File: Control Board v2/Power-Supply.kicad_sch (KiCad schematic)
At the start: 0 parts

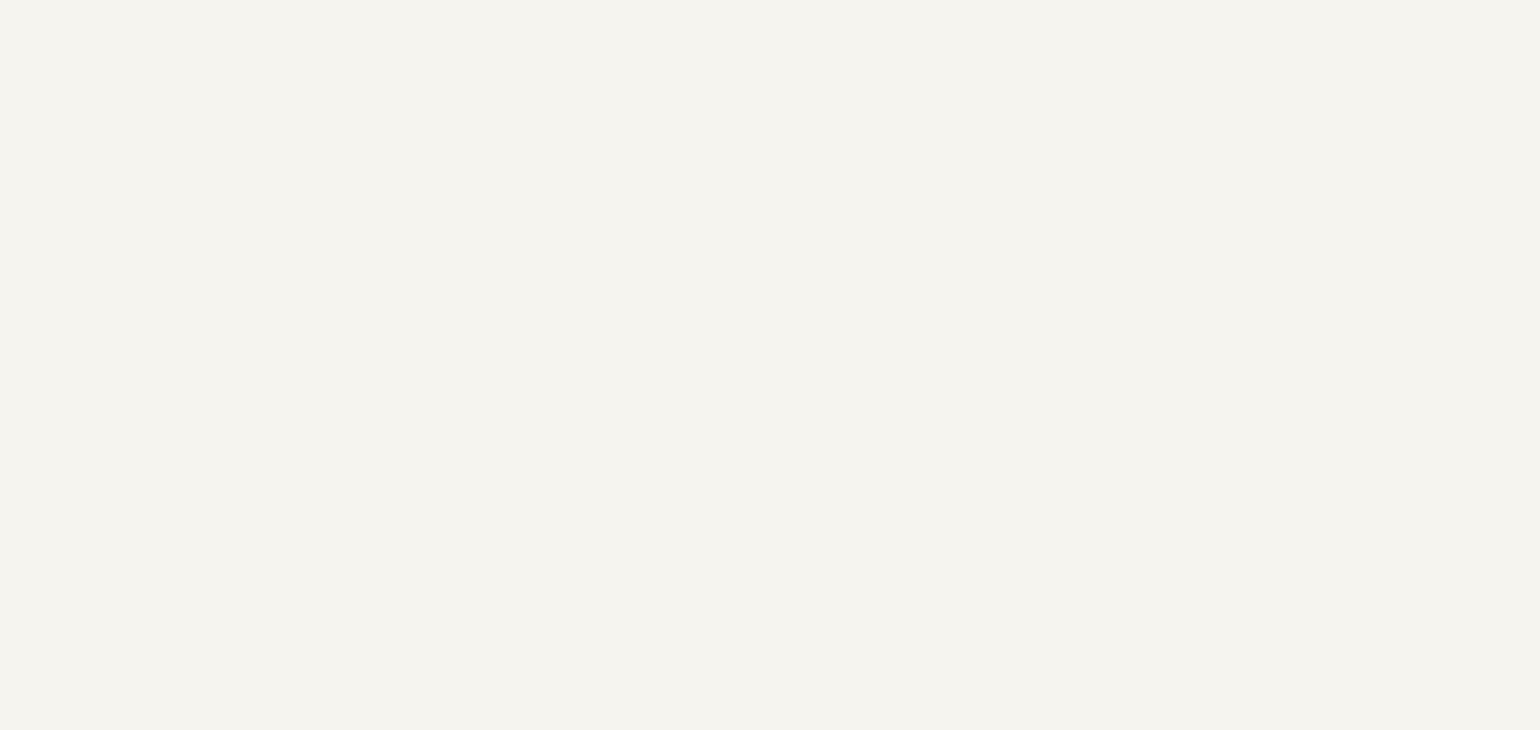
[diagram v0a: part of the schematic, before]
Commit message: Draft power supply and TRIAC driver circuits
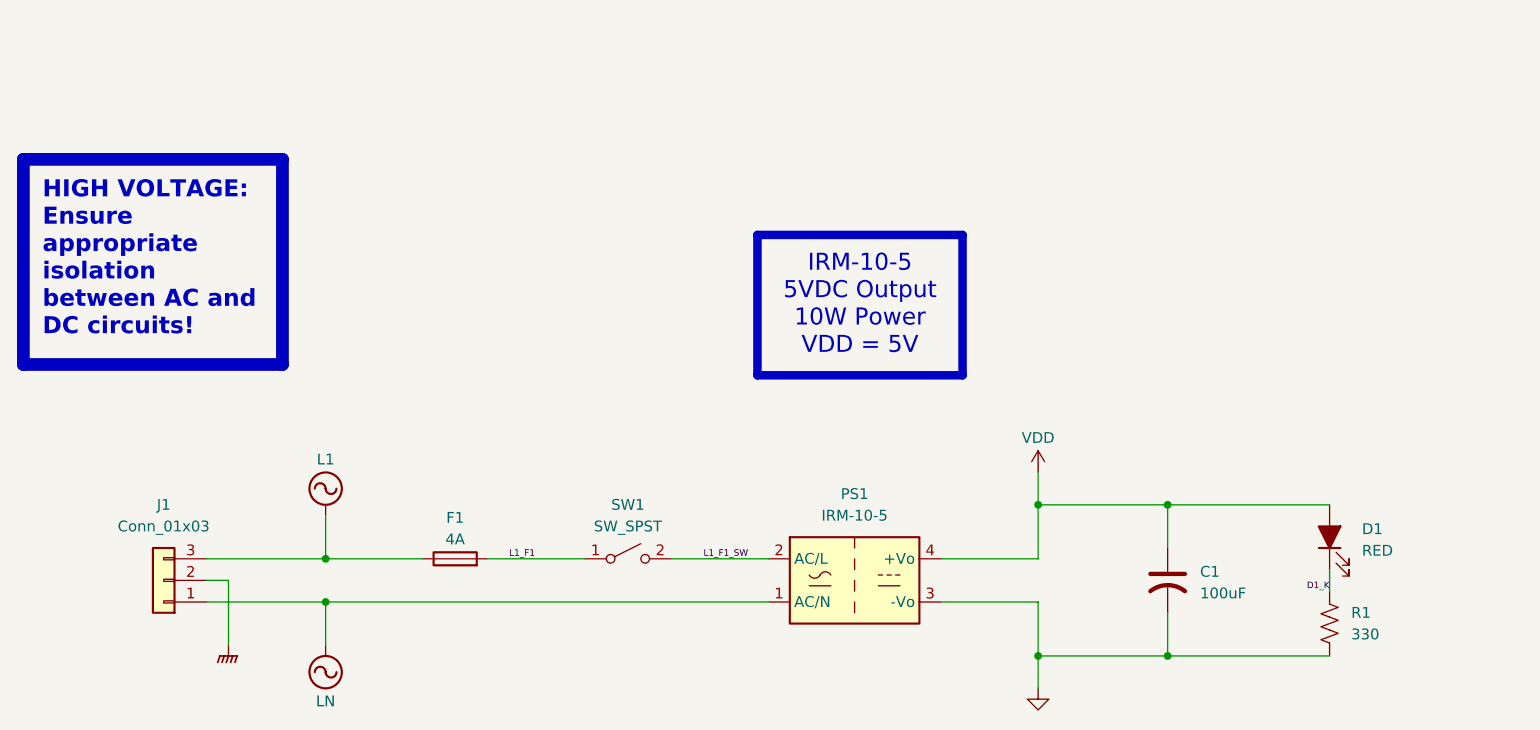
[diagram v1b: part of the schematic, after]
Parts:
- added C1: 100uF, symbol Device:C_US
- added D1: RED, symbol Device:LED_Filled
- added F1: 4A, symbol Device:Fuse
- added J1: Conn_01x03, symbol Connector_Generic:Conn_01x03
- added PS1: IRM-10-5, Converter_ACDC:Converter_ACDC_MeanWell_IRM-10-xx_THT, symbol Converter_ACDC:IRM-10-5
- added R1: 330, symbol Device:R_US
- added SW1: SW_SPST, symbol Switch:SW_SPST
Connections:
- new net D1_K: D1.1 (K), R1.1
- new net GND: C1.2, PS1.3 (-Vo), R1.2
- new net GNDPWR: J1.2 (Pin_2)
- new net L1: F1.1, J1.3 (Pin_3)
- new net L1_F1: F1.2, SW1.1 (A)
- new net L1_F1_SW: PS1.2 (AC/L), SW1.2 (B)
- new net LN: J1.1 (Pin_1), PS1.1 (AC/N)
- new net VDD: C1.1, D1.2 (A), PS1.4 (+Vo)

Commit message: work on PCB layout
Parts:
- added H1, H2, H3, H4: MountingHole_Pad, MountingHole:MountingHole_2.7mm_M2.5_Pad_Via, symbol Mechanical:MountingHole_Pad
- added J6: Conn_01x04, Connector_PinHeader_2.54mm:PinHeader_1x04_P2.54mm_Vertical, symbol Connector_Generic:Conn_01x04
- C1: footprint (none) -> Capacitor_THT:C_Radial_D5.0mm_H5.0mm_P2.00mm
- D1: footprint (none) -> LED_SMD:LED_0603_1608Metric_Pad1.05x0.95mm_HandSolder
- F1: value 4A -> 1A; footprint (none) -> Fuse:Fuse_Blade_ATO_directSolder
- J1: value Conn_01x03 -> 1366005; footprint (none) -> PhoenixContact_SPTA:SPTA-THR 2.53-5.0 P26
- R1: footprint (none) -> Resistor_SMD:R_0603_1608Metric_Pad0.98x0.95mm_HandSolder
- SW1: footprint (none) -> TerminalBlock_Phoenix:TerminalBlock_Phoenix_MKDS-1,5-2-5.08_1x02_P5.08mm_Horizontal
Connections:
- net GND: now also J6.3 (Pin_3), J6.4 (Pin_4)
- net GNDPWR: now also H1.1, H2.1, H3.1, H4.1
- net VDD: now also J6.1 (Pin_1), J6.2 (Pin_2)
